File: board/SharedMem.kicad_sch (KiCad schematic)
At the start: 10 parts, among them U25 HM628512LP-5, U26 74F139, U27 HM628512LP-5, U28 HM628512LP-5, U29 HM628512LP-5

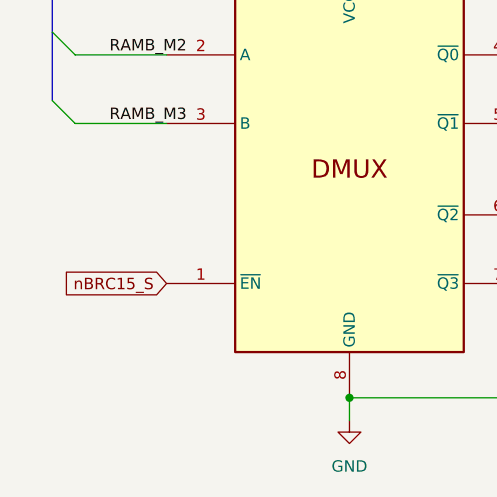
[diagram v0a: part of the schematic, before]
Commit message: V2.0 changes with new S register and simplified logic
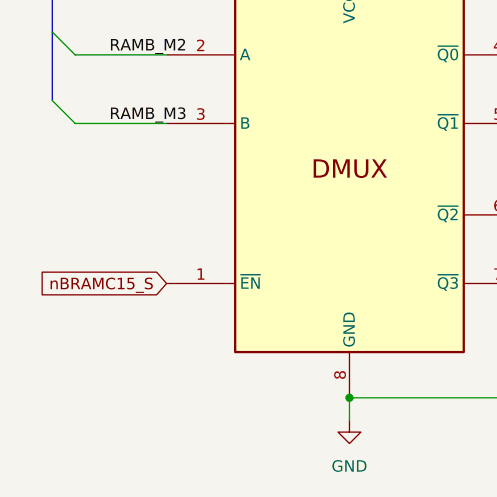
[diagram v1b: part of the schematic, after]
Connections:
- net nBRC15_S renamed nBRAMC15_S
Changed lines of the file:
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@@
 		(title "Shared RAM Banks")
 		(date "2025-10-27")
-		(rev "1.8C")
+		(rev "2.0A")
 		(company "Data Tuning")
 		(comment 1 "Hydra 16")
@@
 		)
 	)
-	(global_label "nBRC15_S"
+	(global_label "nBRAMC15_S"
 		(shape input)
 		(at 30.48 148.59 180)

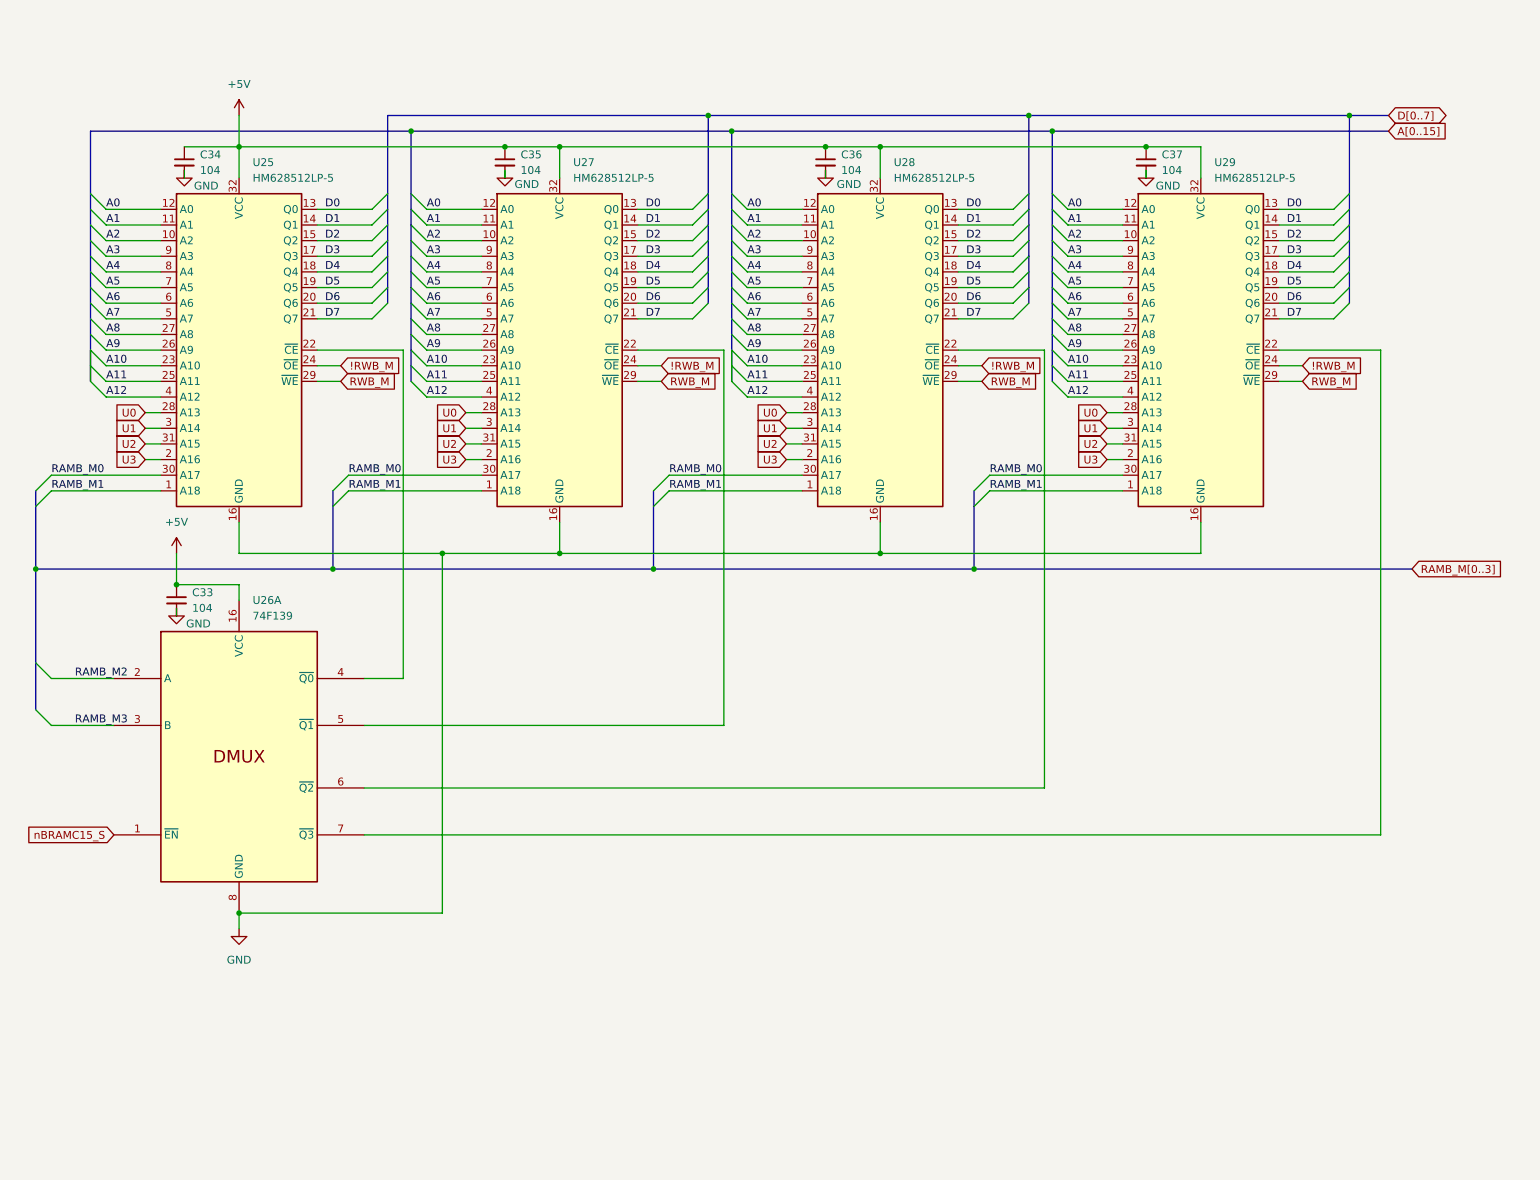
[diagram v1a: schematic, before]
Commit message: V2.0 updates and new hydra breakout and counter cards.
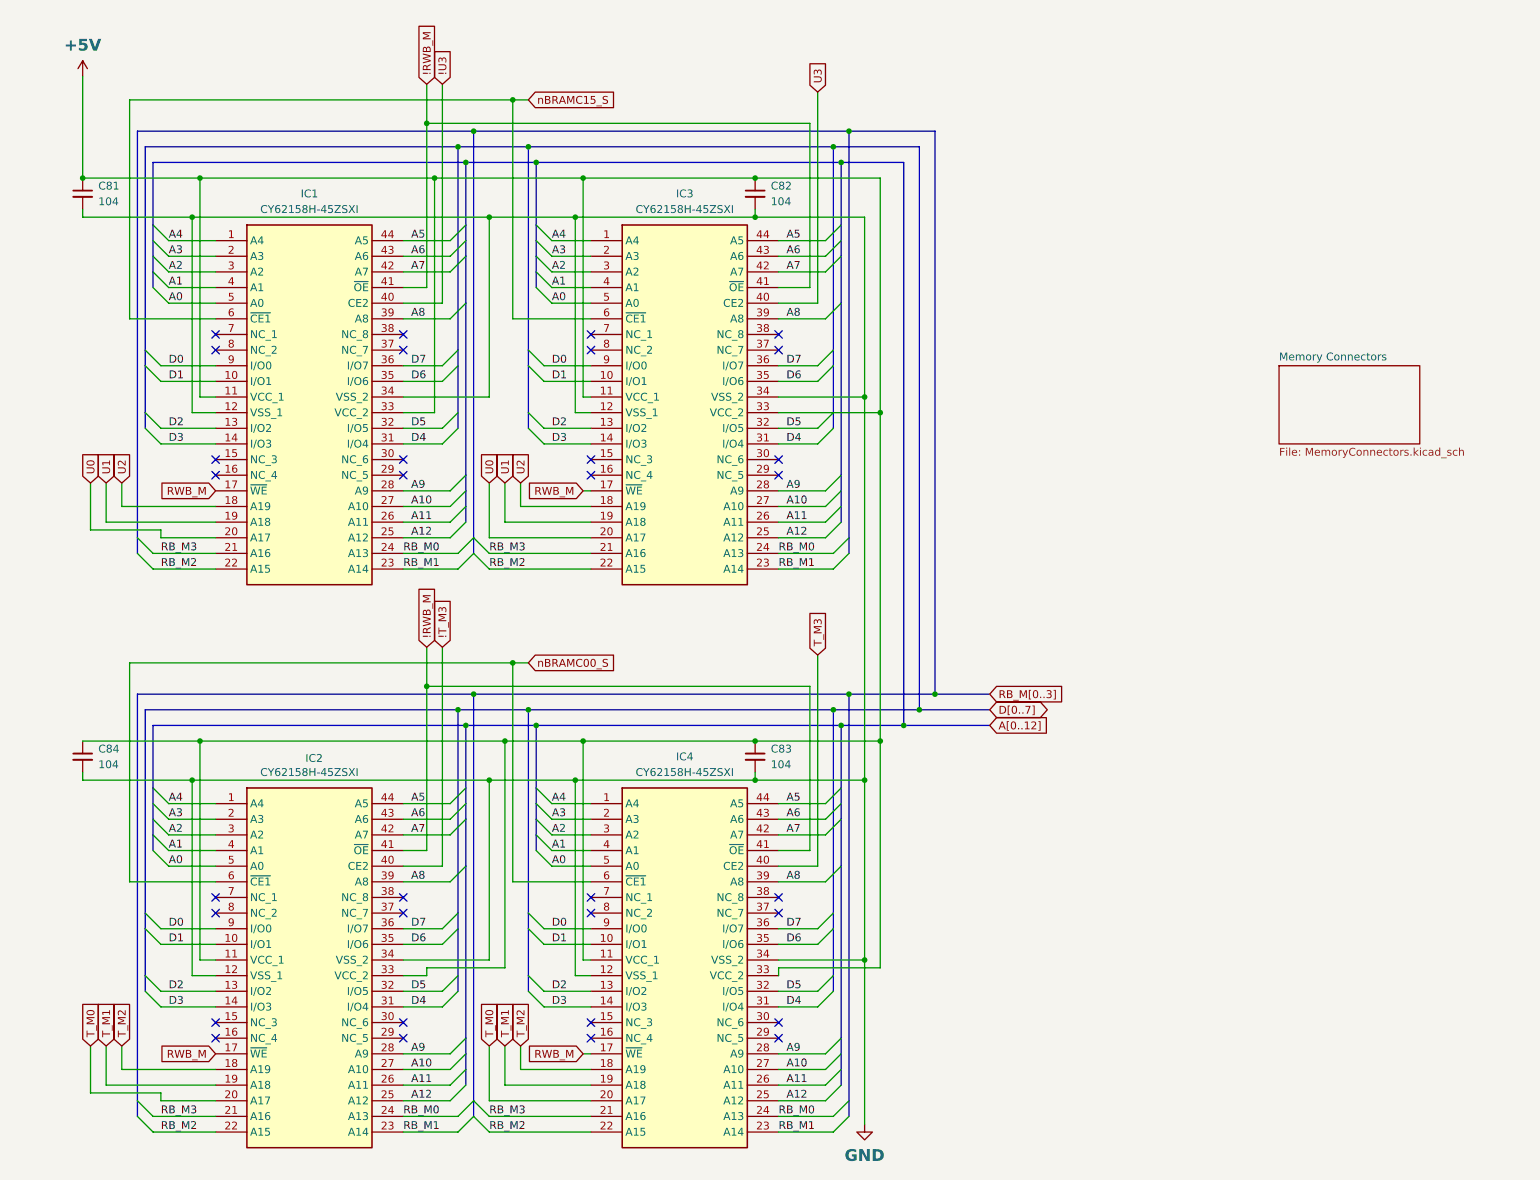
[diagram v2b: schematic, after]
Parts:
- removed C33, C34, C35, C36, C37: 104, Capacitor_THT:C_Disc_D5.0mm_W2.5mm_P5.00mm, symbol Device:C_Small
- removed U25, U27, U28, U29: HM628512LP-5, Package_SO:SOP-32_11.305x20.495mm_P1.27mm, symbol Memory_RAM:628512_DIP32
- removed U26: 74F139, Package_DIP:DIP-16_W7.62mm_Socket_LongPads, symbol 74xx_IEEE:74LS139
- added C81, C82, C83, C84: 104, Capacitor_THT:C_Disc_D5.0mm_W2.5mm_P5.00mm, symbol Device:C_Small
- added IC1, IC2, IC3, IC4: CY62158H-45ZSXI, Package_SO:TSOP-II-44_10.16x18.41mm_P0.8mm, symbol Cypress_Memories:CY62158H-45ZSXI
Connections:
- net !RWB_M: now also IC1.41 (~{OE}), IC2.41 (~{OE}), IC3.41 (~{OE}), IC4.41 (~{OE})
- net +5V: now also C81.1, C82.1, C83.1, C84.1, IC1.11 (VCC_1), IC1.33 (VCC_2), IC2.11 (VCC_1), IC2.33 (VCC_2), IC3.11 (VCC_1), IC3.33 (VCC_2), IC4.11 (VCC_1), IC4.33 (VCC_2)
- net A0: now also IC1.5 (A0), IC2.5 (A0), IC3.5 (A0), IC4.5 (A0)
- net A1: now also IC1.4 (A1), IC2.4 (A1), IC3.4 (A1), IC4.4 (A1)
- net A10: now also IC1.27 (A10), IC2.27 (A10), IC3.27 (A10), IC4.27 (A10)
- net A11: now also IC1.26 (A11), IC2.26 (A11), IC3.26 (A11), IC4.26 (A11)
- net A12: now also IC1.25 (A12), IC2.25 (A12), IC3.25 (A12), IC4.25 (A12)
- net A2: now also IC1.3 (A2), IC2.3 (A2), IC3.3 (A2), IC4.3 (A2)
- net A3: now also IC1.2 (A3), IC2.2 (A3), IC3.2 (A3), IC4.2 (A3)
- net A4: now also IC1.1 (A4), IC2.1 (A4), IC3.1 (A4), IC4.1 (A4)
- net A5: now also IC1.44 (A5), IC2.44 (A5), IC3.44 (A5), IC4.44 (A5)
- net A6: now also IC1.43 (A6), IC2.43 (A6), IC3.43 (A6), IC4.43 (A6)
- net A7: now also IC1.42 (A7), IC2.42 (A7), IC3.42 (A7), IC4.42 (A7)
- net A8: now also IC1.39 (A8), IC2.39 (A8), IC3.39 (A8), IC4.39 (A8)
- net A9: now also IC1.28 (A9), IC2.28 (A9), IC3.28 (A9), IC4.28 (A9)
- net D0: now also IC1.9 (I/O0), IC2.9 (I/O0), IC3.9 (I/O0), IC4.9 (I/O0)
- net D1: now also IC1.10 (I/O1), IC2.10 (I/O1), IC3.10 (I/O1), IC4.10 (I/O1)
- net D2: now also IC1.13 (I/O2), IC2.13 (I/O2), IC3.13 (I/O2), IC4.13 (I/O2)
- net D3: now also IC1.14 (I/O3), IC2.14 (I/O3), IC3.14 (I/O3), IC4.14 (I/O3)
- net D4: now also IC1.31 (I/O4), IC2.31 (I/O4), IC3.31 (I/O4), IC4.31 (I/O4)
- net D5: now also IC1.32 (I/O5), IC2.32 (I/O5), IC3.32 (I/O5), IC4.32 (I/O5)
- net D6: now also IC1.35 (I/O6), IC2.35 (I/O6), IC3.35 (I/O6), IC4.35 (I/O6)
- net D7: now also IC1.36 (I/O7), IC2.36 (I/O7), IC3.36 (I/O7), IC4.36 (I/O7)
- net GND: now also C81.2, C82.2, C83.2, C84.2, IC1.12 (VSS_1), IC1.34 (VSS_2), IC2.12 (VSS_1), IC2.34 (VSS_2), IC3.12 (VSS_1), IC3.34 (VSS_2), IC4.12 (VSS_1), IC4.34 (VSS_2)
- net RWB_M: now also IC1.17 (~{WE}), IC2.17 (~{WE}), IC3.17 (~{WE}), IC4.17 (~{WE})
- net U0: now also IC1.20 (A17), IC3.20 (A17)
- net U1: now also IC1.19 (A18), IC3.19 (A18)
- net U2: now also IC1.18 (A19), IC3.18 (A19)
- net U3: now also IC3.40 (CE2)
- net nBRAMC15_S: now also IC1.6 (~{CE1}), IC3.6 (~{CE1})
- new net !T_M3: IC2.40 (CE2)
- new net !U3: IC1.40 (CE2)
- new net RB_M0: IC1.24 (A13), IC2.24 (A13), IC3.24 (A13), IC4.24 (A13)
- new net RB_M1: IC1.23 (A14), IC2.23 (A14), IC3.23 (A14), IC4.23 (A14)
- new net RB_M2: IC1.22 (A15), IC2.22 (A15), IC3.22 (A15), IC4.22 (A15)
- new net RB_M3: IC1.21 (A16), IC2.21 (A16), IC3.21 (A16), IC4.21 (A16)
- new net T_M0: IC2.20 (A17), IC4.20 (A17)
- new net T_M1: IC2.19 (A18), IC4.19 (A18)
- new net T_M2: IC2.18 (A19), IC4.18 (A19)
- new net T_M3: IC4.40 (CE2)
- new net nBRAMC00_S: IC2.6 (~{CE1}), IC4.6 (~{CE1})
- no-connect marks 0 -> 32
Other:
- added sheet Memory Connectors (MemoryConnectors.kicad_sch)
- title: Shared RAM Banks -> ZeroPage $00/$01 Mirror Memory and RAM/ROM Bank Logic
